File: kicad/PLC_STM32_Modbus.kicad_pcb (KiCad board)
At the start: 2 copper layers, 100 x 80 mm, 314 parts, among them J101 24VDC IN, J201 SWD, J301 USB-C, J401 HR911105A, J402 RS485, J501 OUT 1-8, J502 OUT 9-16, J701 AI 1-10, J702 mA SELECT, J703 AI PWR/COM, Q301 MMBT3904, Q302 MMBT3904, Q303 MMBT3906, Q501 DMN6075S, Q502 DMN6075S, Q503 DMN6075S, Q504 DMN6075S, Q505 DMN6075S, Q506 DMN6075S, Q507 DMN6075S, Q508 DMN6075S, Q509 DMN6075S, Q510 DMN6075S, Q511 DMN6075S, Q512 DMN6075S, Q513 DMN6075S, Q514 DMN6075S, Q515 DMN6075S, Q516 DMN6075S, SW201 RESET, SW202 BOOT, U101 LMR16006YQ5, U102 AMS1117-3.3, U200 STM32F407VET6, U201 REF3030, U301 USBLC6-2SC6, U302 CH340C, U400 W5500, U401 SP3485EN, U501 TLP291-4, U502 TLP291-4, U503 TLP291-4, U504 TLP291-4, Y201 8MHz 20pF, Y401 25MHz 18pF

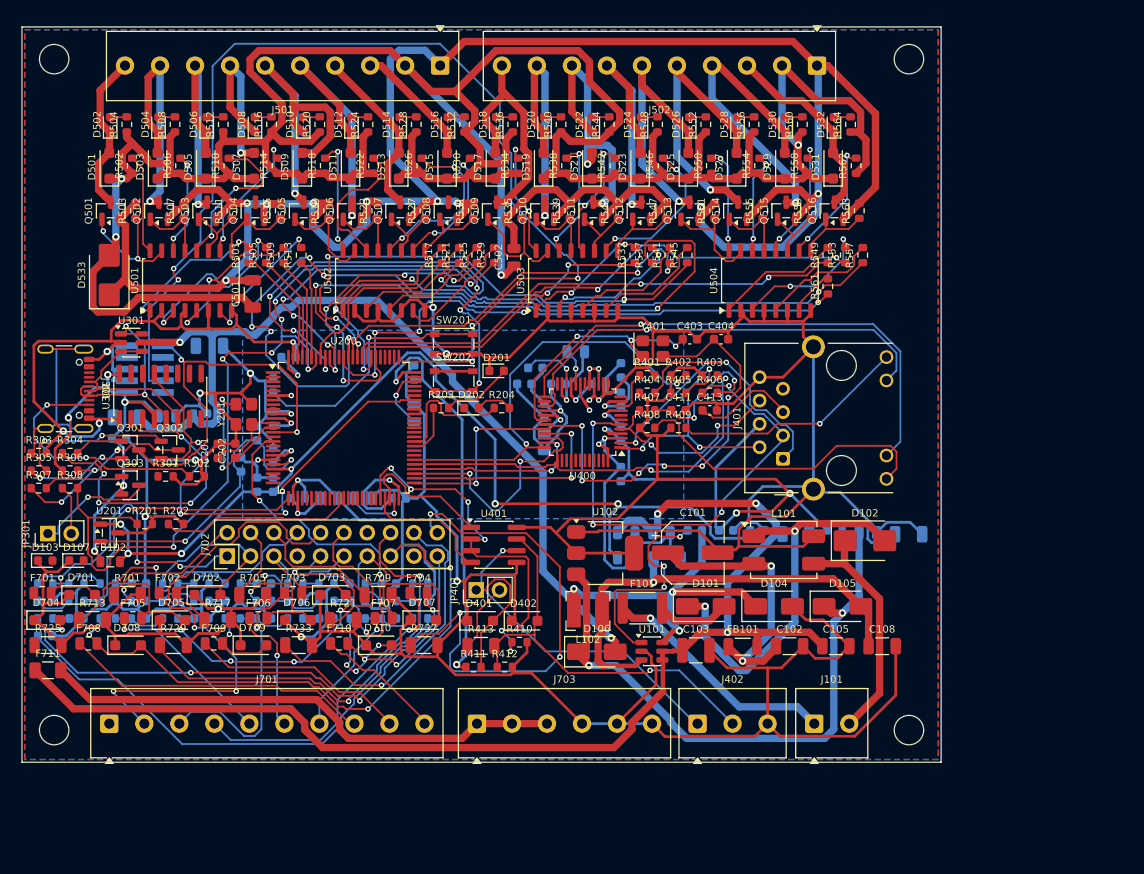
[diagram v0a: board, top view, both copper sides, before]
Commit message: - bỏ các mạch 0-10v, RS485 RTU
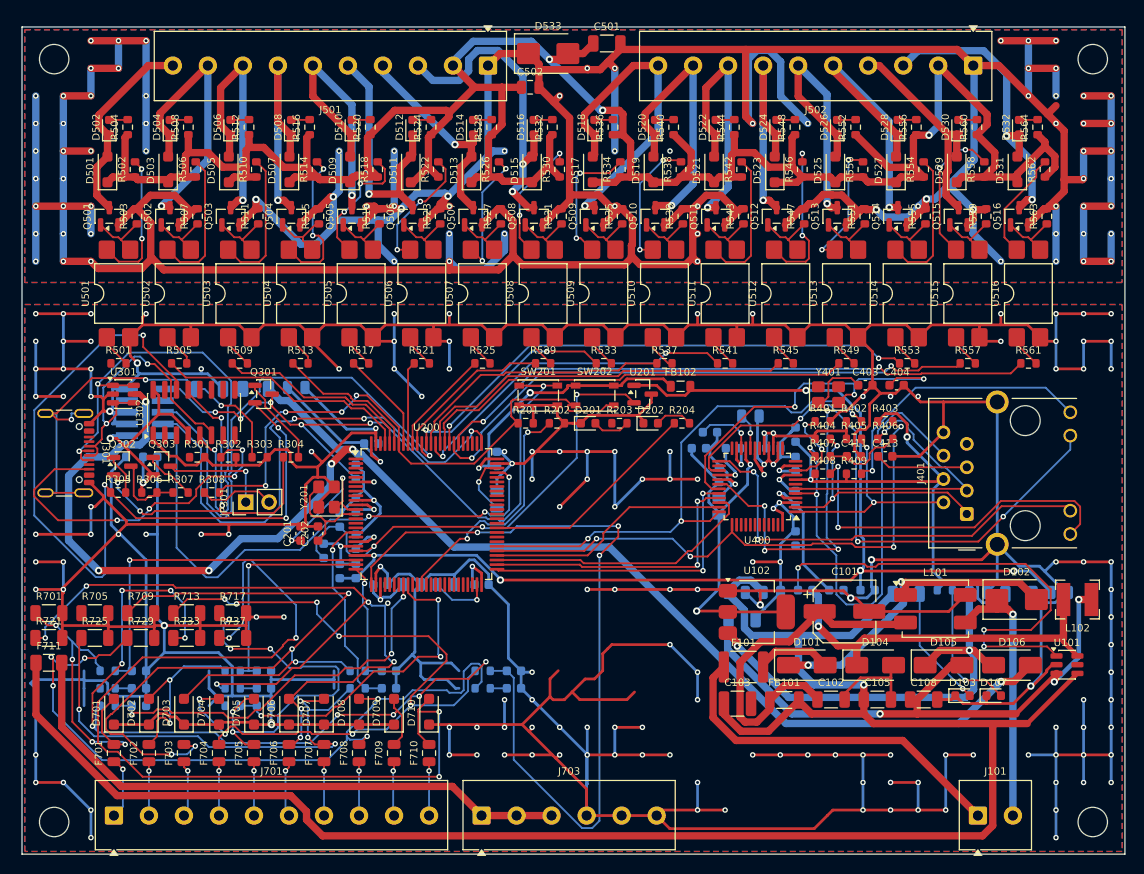
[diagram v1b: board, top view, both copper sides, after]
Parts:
- removed D401, D402: SMF12CA, Diode_SMD:D_SOD-123F
- removed J402: RS485, TerminalBlock_Phoenix:TerminalBlock_Phoenix_MKDS-1-3-3.81_1x03_P3.81mm_Horizontal
- removed J702: mA SELECT, Connector_PinHeader_2.54mm:PinHeader_2x10_P2.54mm_Vertical
- removed JP401: TERM 120R, Connector_PinHeader_2.54mm:PinHeader_1x02_P2.54mm_Vertical
- removed R410: 10k, Resistor_SMD:R_0603_1608Metric
- removed R411, R412: 680, Resistor_SMD:R_0603_1608Metric
- removed R413: 120, Resistor_SMD:R_1206_3216Metric
- removed R702, R706, R710, R714, R718, R722, R726, R730, R734, R738: 47k 0.1%, Resistor_SMD:R_0603_1608Metric
- removed R703, R707, R711, R715, R719, R723, R727, R731, R735, R739: 18k 0.1%, Resistor_SMD:R_0603_1608Metric
- removed U401: SP3485EN, Package_SO:SOIC-8_3.9x4.9mm_P1.27mm
- added U505: PC817 (SMD), Package_DIP:SMDIP-4_W9.53mm, F.Cu at (86.9, 79.0)
- added U506: PC817 (SMD), Package_DIP:SMDIP-4_W9.53mm, F.Cu at (93.5, 79.0)
- added U507: PC817 (SMD), Package_DIP:SMDIP-4_W9.53mm, F.Cu at (100.1, 79.0)
- added U508: PC817 (SMD), Package_DIP:SMDIP-4_W9.53mm, F.Cu at (106.7, 79.0)
- added U509: PC817 (SMD), Package_DIP:SMDIP-4_W9.53mm, F.Cu at (113.3, 79.0)
- added U510: PC817 (SMD), Package_DIP:SMDIP-4_W9.53mm, F.Cu at (119.9, 79.0)
- added U511: PC817 (SMD), Package_DIP:SMDIP-4_W9.53mm, F.Cu at (126.5, 79.0)
- added U512: PC817 (SMD), Package_DIP:SMDIP-4_W9.53mm, F.Cu at (133.1, 79.0)
- added U513: PC817 (SMD), Package_DIP:SMDIP-4_W9.53mm, F.Cu at (139.7, 79.0)
- added U514: PC817 (SMD), Package_DIP:SMDIP-4_W9.53mm, F.Cu at (146.3, 79.0)
- added U515: PC817 (SMD), Package_DIP:SMDIP-4_W9.53mm, F.Cu at (152.9, 79.0)
- added U516: PC817 (SMD), Package_DIP:SMDIP-4_W9.53mm, F.Cu at (159.5, 79.0)
- D701, D702, D703, D704, D705, D706, D707, D708, D709, D710: value SMF12CA -> SMF5.0CA
- J701: value AI 1-10 -> AI 1-10 (4-20mA)
- R701, R705, R709, R713, R717, R721, R725, R729, R733, R737: value 499 0.1% 0.25W -> 120 0.1% 25ppm
- R704, R708, R712, R716, R720, R724, R728, R732, R736, R740: value 1k -> 4.7k
- U501, U502, U503, U504: value TLP291-4 -> PC817 (SMD); footprint Package_SO:SOIC-16_4.55x10.3mm_P1.27mm -> Package_DIP:SMDIP-4_W9.53mm
- moved D107 100.9 mm to (155.7, 122.8)
- moved D103 100.9 mm to (152.3, 122.8)
- moved FB102 64.9 mm to (121.7, 89.1)
- moved U201 60.0 mm to (117.5, 89.9)
- moved D533 53.5 mm to (107.2, 52.9), turned to 0 degrees
- moved L102 53.3 mm to (164.8, 112.3)
- moved U504 51.1 mm to (80.3, 79.0)
- moved C113 47.3 mm to (162.9, 111.5)
- moved C501 47.2 mm to (113.6, 51.8), turned to 0 degrees
- moved D106 45.2 mm to (157.7, 119.4)
- moved U101 45.2 mm to (163.7, 119.4)
- moved C704 44.8 mm to (103.5, 120.1)
- moved R716 44.8 mm to (100.1, 120.1)
- moved R202 42.9 mm to (108.2, 93.1)
- moved R201 42.9 mm to (104.8, 93.1)
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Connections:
- net /Ethernet + RS485/ETH_1V2 renamed /Ethernet/ETH_1V2
- net /Ethernet + RS485/ETH_ACT_LED renamed /Ethernet/ETH_ACT_LED
- net /Ethernet + RS485/ETH_EXRES renamed /Ethernet/ETH_EXRES
- net /Ethernet + RS485/ETH_LEDG_A renamed /Ethernet/ETH_LEDG_A
- net /Ethernet + RS485/ETH_LEDY_A renamed /Ethernet/ETH_LEDY_A
- net /Ethernet + RS485/ETH_LINK_LED renamed /Ethernet/ETH_LINK_LED
- net /Ethernet + RS485/ETH_RCT renamed /Ethernet/ETH_RCT
- net /Ethernet + RS485/ETH_RXMID renamed /Ethernet/ETH_RXMID
- net /Ethernet + RS485/ETH_RXN renamed /Ethernet/ETH_RXN
- net /Ethernet + RS485/ETH_RXP renamed /Ethernet/ETH_RXP
- net /Ethernet + RS485/ETH_TOCAP renamed /Ethernet/ETH_TOCAP
- net /Ethernet + RS485/ETH_TXN renamed /Ethernet/ETH_TXN
- net /Ethernet + RS485/ETH_TXP renamed /Ethernet/ETH_TXP
- net /Ethernet + RS485/ETH_XI renamed /Ethernet/ETH_XI
- net /Ethernet + RS485/ETH_XO renamed /Ethernet/ETH_XO
- R701 pad 1: /10 ngo vao analog/AI1_SH -> /10 ngo vao analog/AI1_IN
- R704 pad 1: Net-(R702-Pad2) -> /10 ngo vao analog/AI1_IN
- R705 pad 1: /10 ngo vao analog/AI2_SH -> /10 ngo vao analog/AI2_IN
- R708 pad 1: Net-(R706-Pad2) -> /10 ngo vao analog/AI2_IN
- R709 pad 1: /10 ngo vao analog/AI3_SH -> /10 ngo vao analog/AI3_IN
- R712 pad 1: Net-(R710-Pad2) -> /10 ngo vao analog/AI3_IN
- R713 pad 1: /10 ngo vao analog/AI4_SH -> /10 ngo vao analog/AI4_IN
- R716 pad 1: Net-(R714-Pad2) -> /10 ngo vao analog/AI4_IN
- R717 pad 1: /10 ngo vao analog/AI5_SH -> /10 ngo vao analog/AI5_IN
- R720 pad 1: Net-(R718-Pad2) -> /10 ngo vao analog/AI5_IN
- R721 pad 1: /10 ngo vao analog/AI6_SH -> /10 ngo vao analog/AI6_IN
- R724 pad 1: Net-(R722-Pad2) -> /10 ngo vao analog/AI6_IN
- R725 pad 1: /10 ngo vao analog/AI7_SH -> /10 ngo vao analog/AI7_IN
- R728 pad 1: Net-(R726-Pad2) -> /10 ngo vao analog/AI7_IN
- R729 pad 1: /10 ngo vao analog/AI8_SH -> /10 ngo vao analog/AI8_IN
- R732 pad 1: Net-(R730-Pad2) -> /10 ngo vao analog/AI8_IN
- R733 pad 1: /10 ngo vao analog/AI9_SH -> /10 ngo vao analog/AI9_IN
- R736 pad 1: Net-(R734-Pad2) -> /10 ngo vao analog/AI9_IN
- R737 pad 1: /10 ngo vao analog/AI10_SH -> /10 ngo vao analog/AI10_IN
- R740 pad 1: Net-(R738-Pad2) -> /10 ngo vao analog/AI10_IN
- U200 pad 46: RS485_DE -> unconnected-(U200-PE15-Pad46)
- U200 pad 47: RS485_TX -> unconnected-(U200-PB10-Pad47)
- U200 pad 48: RS485_RX -> unconnected-(U200-PB11-Pad48)
- U501 pad 3: Net-(R505-Pad2) -> Net-(Q501-G)
- U501 pad 4: GND -> Net-(R502-Pad2)
- U502 pad 1: Net-(R517-Pad2) -> Net-(R505-Pad2)
- U502 pad 3: Net-(R521-Pad2) -> Net-(Q502-G)
- U502 pad 4: GND -> Net-(R506-Pad2)
- U503 pad 1: Net-(R533-Pad2) -> Net-(R509-Pad2)
- U503 pad 3: Net-(R537-Pad2) -> Net-(Q503-G)
- U503 pad 4: GND -> Net-(R510-Pad2)
- U504 pad 1: Net-(R549-Pad2) -> Net-(R513-Pad2)
- U504 pad 3: Net-(R553-Pad2) -> Net-(Q504-G)
- U504 pad 4: GND -> Net-(R514-Pad2)
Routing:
- net GND: track 786.5 -> 1231.1 mm, vias 24 -> 159
- net /16 ngo ra transistor/COM_OUT: track 268.7 -> 572.6 mm, vias 9 -> 82
- net /USB nap code/CH_RTS: track 11.2 -> 89.8 mm, vias 2 -> 4
- net /10 ngo vao analog/AI3_IN: track 14.1 -> 92.6 mm, vias 0 -> 5
- net +24V: track 136.9 -> 215.0 mm, vias 3 -> 1
- net /10 ngo vao analog/AI9_IN: track 8.81 -> 84.8 mm, vias 1 -> 9
- net /10 ngo vao analog/AI10_IN: track 32.0 -> 104.2 mm, vias 5 -> 4
- net VBUS: track 97.1 -> 162.7 mm, vias 2 -> 6
- net /MCU STM32F407VET6/SWCLK: track 122.4 -> 58.6 mm, vias 5 -> 3
- net /10 ngo vao analog/AI6_IN: track 27.0 -> 90.0 mm, vias 2 -> 8
- net DO10: track 90.9 -> 29.4 mm, vias 6 -> 0
- net /MCU STM32F407VET6/SWDIO: track 0.00 -> 59.7 mm, vias 0 -> 3
- net +3V3: track 280.6 -> 222.7 mm, vias 21 -> 19
- net AI4_ADC: track 31.2 -> 88.1 mm, vias 1 -> 3
- net /MCU STM32F407VET6/SWO: track 0.00 -> 56.1 mm, vias 0 -> 1
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- added copper zone on B.Cu, net /16 ngo ra transistor/COM_OUT
- added copper zone on F.Cu, net /16 ngo ra transistor/COM_OUT
- removed copper zone on B.Cu, net +3V3
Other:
- board size 100 x 80 mm -> 120 x 90 mm
- board text added: "PLC STM32F407 MODBUS TCP - 16DO/10AI v1.1"
- board text removed: "PLC STM32F407 MODBUS TCP - 16DO/10AI v1.0"

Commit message: - bỏ các cầu chì thêm mô tả cho từng linh kiên
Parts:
- removed F701, F702, F703, F704, F705, F706, F707, F708, F709, F710: 50mA, Fuse:Fuse_0805_2012Metric
- F711: value 200mA -> MF-MSMF050-2 0.5A/60V; footprint Fuse:Fuse_1206_3216Metric -> Fuse:Fuse_1812_4532Metric
- moved F711 49.7 mm to (102.5, 116.0)
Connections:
- J701 pad 1: /10 ngo vao analog/AI1_T -> /10 ngo vao analog/AI1_IN
- J701 pad 10: /10 ngo vao analog/AI10_T -> /10 ngo vao analog/AI10_IN
- J701 pad 2: /10 ngo vao analog/AI2_T -> /10 ngo vao analog/AI2_IN
- J701 pad 3: /10 ngo vao analog/AI3_T -> /10 ngo vao analog/AI3_IN
- J701 pad 4: /10 ngo vao analog/AI4_T -> /10 ngo vao analog/AI4_IN
- J701 pad 5: /10 ngo vao analog/AI5_T -> /10 ngo vao analog/AI5_IN
- J701 pad 6: /10 ngo vao analog/AI6_T -> /10 ngo vao analog/AI6_IN
- J701 pad 7: /10 ngo vao analog/AI7_T -> /10 ngo vao analog/AI7_IN
- J701 pad 8: /10 ngo vao analog/AI8_T -> /10 ngo vao analog/AI8_IN
- J701 pad 9: /10 ngo vao analog/AI9_T -> /10 ngo vao analog/AI9_IN
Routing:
- net +24V: track 215.0 -> 118.3 mm, vias 1 -> 2
- net /10 ngo vao analog/AI2_IN: track 19.4 -> 69.5 mm, vias 2 -> 5
- net /10 ngo vao analog/V24_LOOP: track 64.3 -> 36.4 mm
- net /10 ngo vao analog/AI4_IN: track 81.6 -> 102.7 mm
- net /10 ngo vao analog/AI1_IN: track 32.9 -> 43.5 mm, vias 4 -> 5
- net /10 ngo vao analog/AI10_IN: track 104.2 -> 112.4 mm
- net /10 ngo vao analog/AI7_IN: track 54.3 -> 62.1 mm, vias 4 -> 5
- net /10 ngo vao analog/AI6_IN: track 90.0 -> 97.6 mm, vias 8 -> 9
- net /10 ngo vao analog/AI1_T: track 6.77 -> 0.00 mm, vias 1 -> 0
- net /10 ngo vao analog/AI5_IN: track 42.4 -> 48.9 mm, vias 5 -> 6
- net /10 ngo vao analog/AI3_T: track 6.21 -> 0.00 mm, vias 1 -> 0
- net /10 ngo vao analog/AI6_T: track 6.18 -> 0.00 mm, vias 1 -> 0
- net /10 ngo vao analog/AI9_T: track 5.94 -> 0.00 mm, vias 1 -> 0
- net /10 ngo vao analog/AI8_T: track 5.86 -> 0.00 mm, vias 1 -> 0
- net /10 ngo vao analog/AI7_T: track 5.86 -> 0.00 mm, vias 1 -> 0
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
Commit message: - thay w5500 bằng module w5500 lite
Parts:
- removed C403, C404: 18pF, Capacitor_SMD:C_0603_1608Metric
- removed C405, C406, C407, C408, C409, C414, C415: 100nF, Capacitor_SMD:C_0603_1608Metric
- removed C410: 10uF, Capacitor_SMD:C_0805_2012Metric
- removed C411: 6.8nF, Capacitor_SMD:C_0603_1608Metric
- removed C412, C413: 10nF, Capacitor_SMD:C_0603_1608Metric
- removed R403: 10k, Resistor_SMD:R_0603_1608Metric
- removed R404, R405, R406, R407: 49.9 1%, Resistor_SMD:R_0603_1608Metric
- removed R408, R409: 330, Resistor_SMD:R_0603_1608Metric
- removed U400: W5500, Package_QFP:LQFP-48_7x7mm_P0.5mm
- removed Y401: 25MHz 18pF, Crystal:Crystal_SMD_3225-4Pin_3.2x2.5mm
- C401: value 4.7uF -> 10uF
- C402: value 10nF -> 100nF
- J401: value HR911105A -> W5500 Lite module; footprint Connector_RJ:RJ45_Hanrun_HR911105A_Horizontal -> PLC:W5500_Lite_Module
- R401: value 12.4k 1% -> 10k; moved to B.Cu
- R402: moved to B.Cu
- moved C402 33.4 mm to (155.9, 106.4), turned to 90 degrees
- moved C401 32.4 mm to (158.4, 106.4), turned to 90 degrees
- moved R402 16.9 mm to (150.8, 106.4), turned to 90 degrees
- moved J401 16.0 mm to (161.0, 89.2), turned to -90 degrees
- moved R401 11.1 mm to (148.3, 92.4), turned to 90 degrees
- moved C101 1.20 mm to (139.5, 114.8)
- moved C102 1.20 mm to (138.0, 124.4)
- moved C103 1.20 mm to (127.8, 124.8)
- moved C105 1.20 mm to (143.1, 124.4)
- moved C108 1.20 mm to (148.1, 124.4)
- moved C109 1.20 mm to (128.3, 115.6)
- moved C111 1.20 mm to (158.5, 112.9)
- moved D101 1.20 mm to (135.4, 120.6)
- moved D102 1.20 mm to (158.2, 113.5)
- moved D103 1.20 mm to (152.3, 124.0)
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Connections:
- C401 pad 1: /Ethernet/ETH_TOCAP -> +3V3
- C402 pad 1: /Ethernet/ETH_1V2 -> +3V3
- J401 pad 1: /Ethernet/ETH_TXP -> GND
- J401 pad 10: /Ethernet/ETH_LINK_LED -> unconnected-(J401-NC-Pad10)
- J401 pad 11: /Ethernet/ETH_ACT_LED -> ETH_RST
- J401 pad 12: /Ethernet/ETH_LEDY_A -> ETH_MISO
- J401 pad 2: /Ethernet/ETH_TXN -> GND
- J401 pad 3: /Ethernet/ETH_RXP -> ETH_MOSI
- J401 pad 4: +3V3 -> ETH_SCK
- J401 pad 5: /Ethernet/ETH_RCT -> ETH_CS
- J401 pad 6: /Ethernet/ETH_RXN -> ETH_INT
- J401 pad 7: unconnected-(J401-NC-Pad7) -> GND
- J401 pad 8: GND -> +3V3
- J401 pad 9: /Ethernet/ETH_LEDG_A -> +3V3
- R401 pad 1: /Ethernet/ETH_EXRES -> +3V3
- R401 pad 2: GND -> ETH_INT
- R402 pad 2: ETH_INT -> ETH_RST
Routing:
- net VBUS: track 162.7 -> 74.0 mm, vias 6 -> 5
- net /Ethernet/ETH_ACT_LED: track 62.8 -> 0.00 mm, vias 3 -> 0
- net /Ethernet/ETH_RXN: track 54.4 -> 0.00 mm, vias 2 -> 0
- net /Ethernet/ETH_LINK_LED: track 47.5 -> 0.00 mm, vias 2 -> 0
- net /Nguon 24VDC/BUCK_CB: track 52.1 -> 8.32 mm, vias 3 -> 0
- net /Ethernet/ETH_XI: track 42.3 -> 0.00 mm, vias 4 -> 0
- net /Ethernet/ETH_XO: track 40.2 -> 0.00 mm, vias 3 -> 0
- net /Nguon 24VDC/VIN_RAW: track 40.0 -> 0.00 mm
- net /10 ngo vao analog/AI5_IN: track 48.9 -> 88.7 mm, vias 6 -> 10
- net /Ethernet/ETH_LEDG_A: track 39.0 -> 0.00 mm, vias 2 -> 0
- net ETH_SCK: track 31.4 -> 67.6 mm
- net /Ethernet/ETH_RXP: track 33.1 -> 0.00 mm, vias 1 -> 0
- net ETH_CS: track 32.7 -> 65.3 mm
- net /Ethernet/ETH_LEDY_A: track 30.2 -> 0.00 mm, vias 1 -> 0
- net ETH_MISO: track 29.7 -> 0.00 mm
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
